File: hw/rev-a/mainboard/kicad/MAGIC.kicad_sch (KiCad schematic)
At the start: 16 parts, among them U7 SN74LVC4245APWR, U8 SN74LVC4245APWR, U9 SN74LVC4245APWR

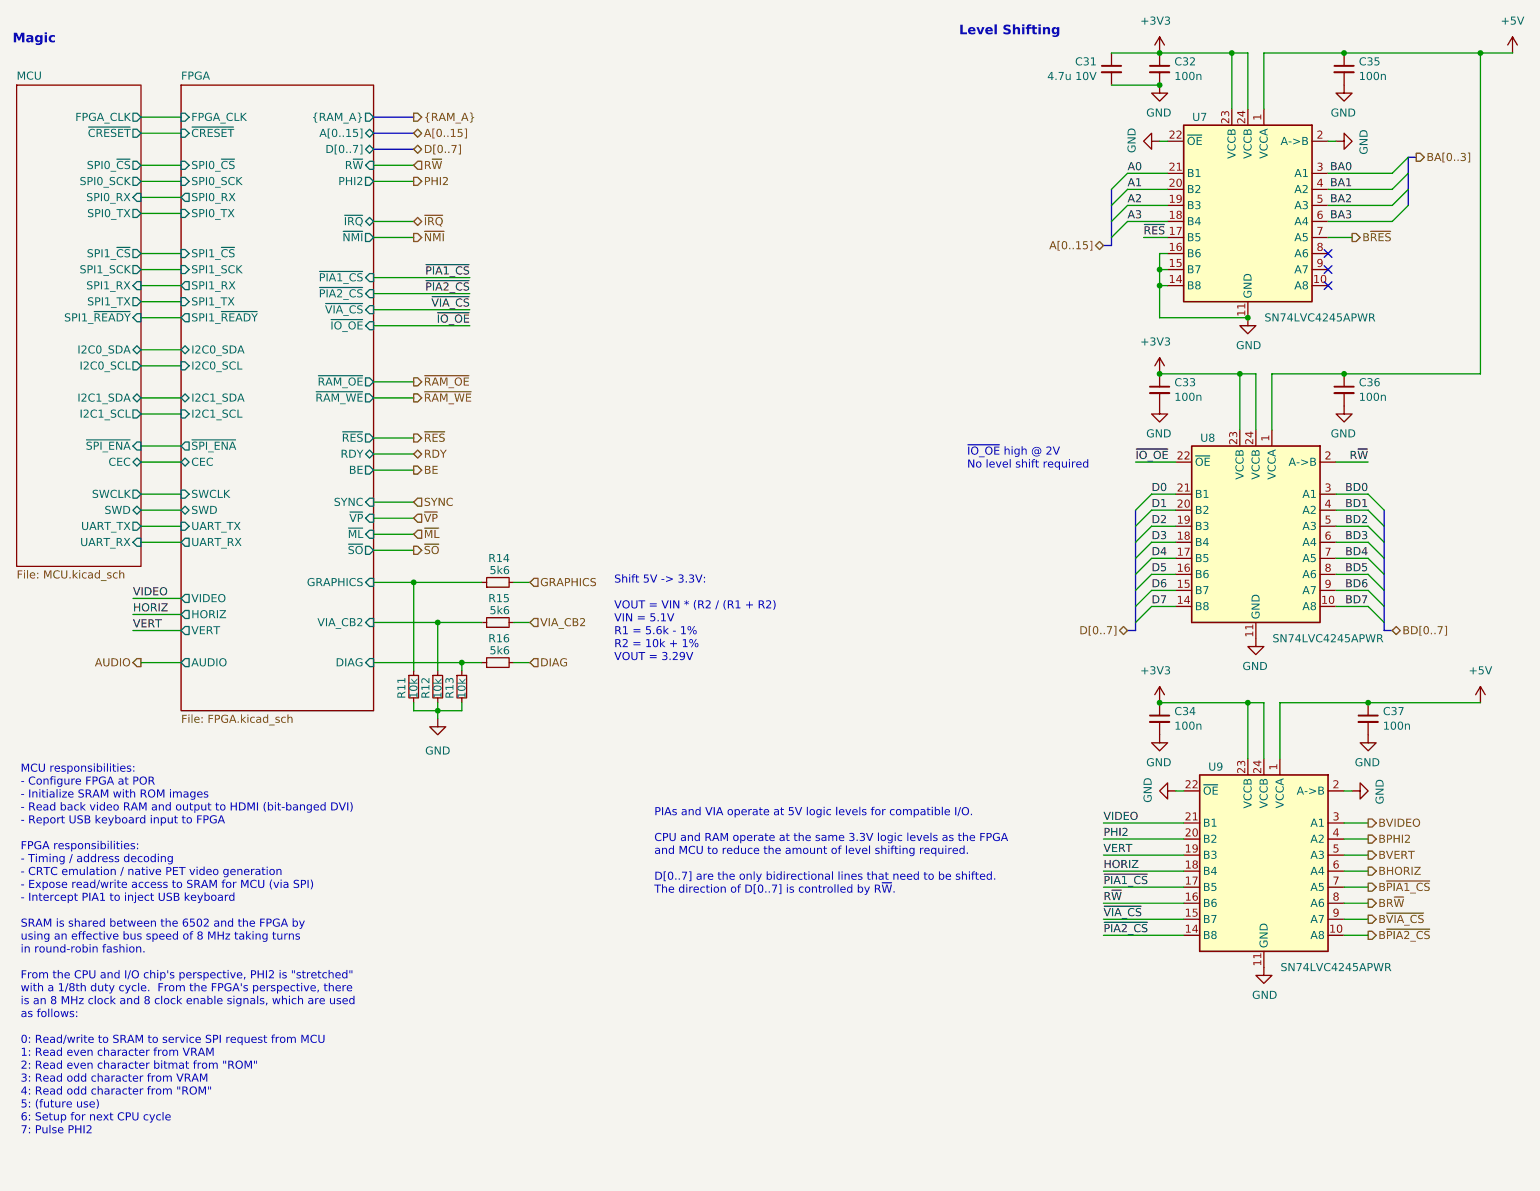
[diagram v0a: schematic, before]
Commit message: hw: ren rev-c -> rev-a
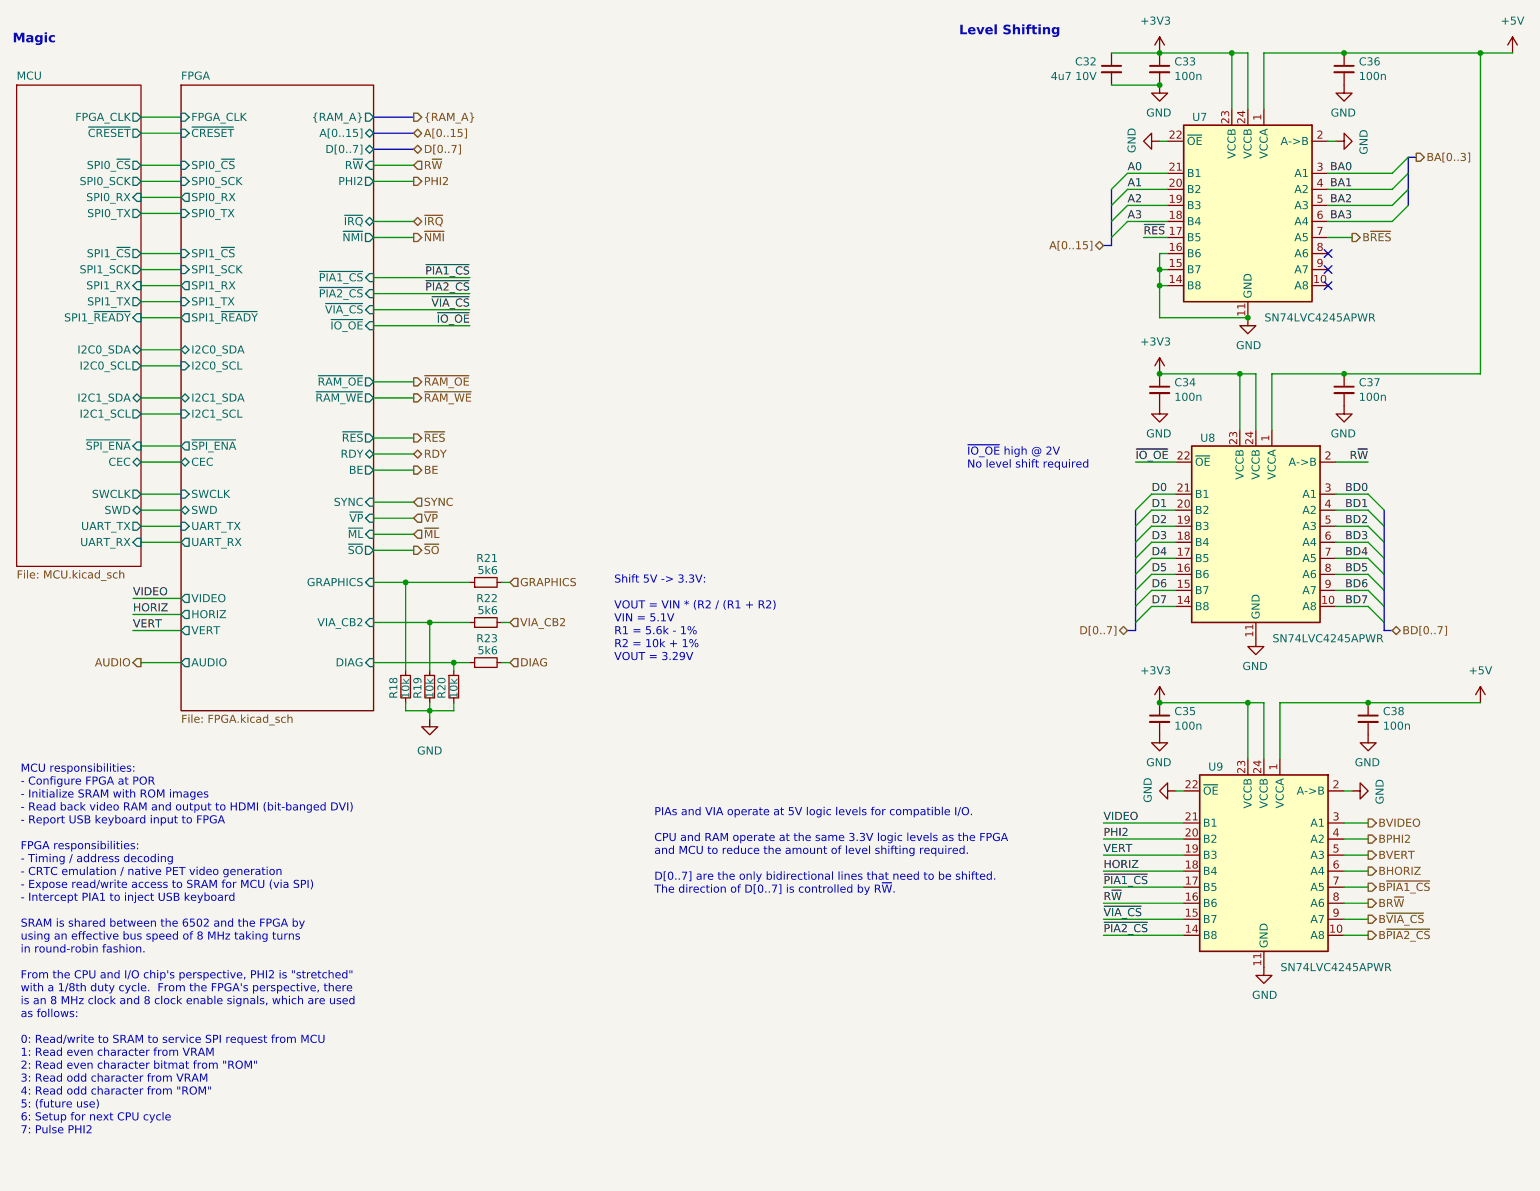
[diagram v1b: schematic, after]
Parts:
- C32: renamed from C31; value 4.7u 10V -> 4u7 10V
- U7, U8, U9: symbol Mainboard-rescue:SN74LVC8T245-PET -> EconoPET:SN74LVC8T245
- renumbered C32 to C33, C33 to C34, C34 to C35, C35 to C36, C36 to C37, C37 to C38, R11 to R18, R12 to R19, R13 to R20, R14 to R21, R15 to R22, R16 to R23
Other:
- moved on the sheet: R18, R19, R20, R21, R22, R23

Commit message: hw: tidy schematics for publication
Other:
- note added: "MCU responsibilities: - Generate FPGA_CLK - Configure FPGA at POR - Initialize SRAM with ROM images - Read back video RAM and output to HDMI (bit-banged DVI) - Report USB keyboard matrix to FPGA FPGA responsibilities: - Timing / address decoding - Native PET video generation / CRTC - Expose sysem bus to MCU (via SPI) - Intercept PIA1 to inject USB keyboard SRAM is shared between the 6502 and the 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"
- note added: "PIAs and VIA operate at 5V logic levels for compatible I/O. CPU and RAM operate at the same 3V3 logic levels as the FPGA and MCU to reduce the amount of level shifting required. D[0..7] are the only bidirectional lines that need to be shifted. The direction of D[0..7] is controlled by R~{W}."
- note added: "Shift 5V -> 3V3: VOUT = VIN * (R2 / (R1 + R2) VIN = 5.1V R1 = 5.6k - 1% R2 = 10k + 1% VOUT = 3.29V"
- note added: "~{IO_OE} does not require level-shifting (high @ 2V)"
- note removed: "MCU responsibilities: - Configure FPGA at POR - Initialize SRAM with ROM images - Read back video RAM and output to HDMI (bit-banged DVI) - Report USB keyboard input to FPGA FPGA responsibilities: - Timing / address decoding - CRTC emulation / native PET video generation - Expose read/write access to SRAM for MCU (via SPI) - Intercept PIA1 to inject USB keyboard SRAM is shared between the 6502 an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"
- note removed: "PIAs and VIA operate at 5V logic levels for compatible I/O. CPU and RAM operate at the same 3.3V logic levels as the FPGA and MCU to reduce the amount of level shifting required. D[0..7] are the only bidirectional lines that need to be shifted. The direction of D[0..7] is controlled by R~{W}."
- note removed: "Shift 5V -> 3.3V: VOUT = VIN * (R2 / (R1 + R2) VIN = 5.1V R1 = 5.6k - 1% R2 = 10k + 1% VOUT = 3.29V"
- note removed: "~{IO_OE} high @ 2V No level shift required"
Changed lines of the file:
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@@
 		(date "2023-10-01")
 		(rev "A")
+		(comment 1 "Unspecified resistors are 1% and rated for 62.5mW or higher")
+		(comment 2 "Unspecified capacitors are rated for 25V or higher")
+		(comment 3 "Signals with B-prefix are level-shifted from 3V3 to 5V")
 	)
 	(junction
@@
 		)
 	)
-	(text "PIAs and VIA operate at 5V logic levels for compatible I/O.\n\nCPU and RAM operate at the same 3.3V logic levels as the FPGA\nand MCU to reduce the amount of level shifting required.\n\nD[0..7] are the only bidirectional lines that need to be shifted.\nThe direction of D[0..7] is controlled by R~{W}."
+	(text "PIAs and VIA operate at 5V logic levels for compatible I/O.\n\nCPU and RAM operate at the same 3V3 logic levels as the FPGA\nand MCU to reduce the amount of level shifting required.\n\nD[0..7] are the only bidirectional lines that need to be shifted.\nThe direction of D[0..7] is controlled by R~{W}."
 		(exclude_from_sim no)
 		(at 127 153.67 0)
@@
 		)
 	)
-	(text "MCU responsibilities:\n- Configure FPGA at POR\n- Initialize SRAM with ROM images\n- Read back video RAM and output to HDMI (bit-banged DVI)\n- Report USB keyboard input to FPGA\n\nFPGA responsibilities:\n- Timing / address decoding\n- CRTC emulation / native PET video generation\n- Expose read/write access to SRAM for MCU (via SPI)\n- Intercept PIA1 to inject USB keyboard\n\nSRAM is shared between the 6502 and the FPGA by\nusing an effective bus speed of 8 MHz taking turns\nin round-robin fashion.\n\nFrom the CPU and I/O chip's perspective, PHI2 is \"stretched\"\nwith a 1/8th duty cycle.  From the FPGA's perspective, there\nis an 8 MHz clock and 8 clock enable signals, which are used\nas follows:\n\n0: Read/write to SRAM to service SPI request from MCU\n1: Read even character from VRAM\n2: Read even character bitmat from \"ROM\"\n3: Read odd character from VRAM\n4: Read odd character from \"ROM\"\n5: (future use)\n6: Setup for next CPU cycle\n7: Pulse PHI2"
+	(text "MCU responsibilities:\n- Generate FPGA_CLK\n- Configure FPGA at POR\n- Initialize SRAM with ROM images\n- Read back video RAM and output to HDMI (bit-banged DVI)\n- Report USB keyboard matrix to FPGA\n\nFPGA responsibilities:\n- Timing / address decoding\n- Native PET video generation / CRTC\n- Expose sysem bus to MCU (via SPI)\n- Intercept PIA1 to inject USB keyboard\n\nSRAM is shared between the 6502 and the FPGA by using an\neffective bus speed of 8 MHz taking turns in round-robin\nfashion.\n\nFrom the CPU and I/O chip's perspective, PHI2 is \"stretched\"\nwith a 1/8th duty cycle.  From the FPGA's perspective, there\nis an 8 MHz clock and 8 clock enable signals, which are used\nas follows:\n\n0: Read/write to SRAM to service SPI request from MCU\n1: Read even character from VRAM\n2: Read even character bitmat from \"ROM\"\n3: Read odd character from VRAM\n4: Read odd character from \"ROM\"\n5: Read/write to SRAM to service SPI request from MCU\n6: Setup for next CPU cycle\n7: Pulse PHI2\n\n(Note: Above subject to change with firmware updates.)"
 		(exclude_from_sim no)
-		(at 26.67 191.77 0)
+		(at 26.67 198.12 0)
 		(effects
 			(font
@@
 		)
 	)
-	(text "~{IO_OE} high @ 2V\nNo level shift required"
+	(text "~{IO_OE} does not require level-shifting\n(high @ 2V)"
 		(exclude_from_sim no)
-		(at 176.53 86.36 0)
+		(at 163.83 85.09 0)
 		(effects
 			(font
@@
 		)
 	)
-	(text "Shift 5V -> 3.3V:\n\nVOUT = VIN * (R2 / (R1 + R2)\nVIN = 5.1V\nR1 = 5.6k - 1%\nR2 = 10k + 1%\nVOUT = 3.29V"
+	(text "Shift 5V -> 3V3:\n\nVOUT = VIN * (R2 / (R1 + R2)\nVIN = 5.1V\nR1 = 5.6k - 1%\nR2 = 10k + 1%\nVOUT = 3.29V"
 		(exclude_from_sim no)
 		(at 120.65 116.84 0)

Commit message: hw: tidy schematics for publication
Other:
- company: (none) -> https://is.gd/6hpvh6
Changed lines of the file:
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@@
 		(date "2023-10-01")
 		(rev "A")
-		(comment 1 "Unspecified resistors are 1% and rated for 62.5mW or higher")
-		(comment 2 "Unspecified capacitors are rated for 25V or higher")
+		(company "https://is.gd/6hpvh6")
+		(comment 1 "Unspecified resistors are 1% / 62.5mW")
+		(comment 2 "Unspecified capacitors are 25V")
 		(comment 3 "Signals with B-prefix are level-shifted from 3V3 to 5V")
+		(comment 4 "License: CC0 1.0 Universal (Public Domain Dedication)")
 	)
 	(junction

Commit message: hw: tidy schematics for publication
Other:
- note added: "PIAs and VIA operate at 5V logic levels for compatible I/O. To reduce the amount of level shifting required, CPU and RAM operate at 3V3 logic levels to share the system bus with the FPGA. D[0..7] are the only bidirectional lines that need to be shifted. The direction of D[0..7] is controlled by R~{W}."
- note added: "~{IO_OE} is asserted whenenver address decoding asserts ~{PIA1_CS}, ~{PIA2_CS}, or ~{VIA_CS}. ~{IO_OE} does not require level-shifting (high @ 2V)"
- note removed: "PIAs and VIA operate at 5V logic levels for compatible I/O. CPU and RAM operate at the same 3V3 logic levels as the FPGA and MCU to reduce the amount of level shifting required. D[0..7] are the only bidirectional lines that need to be shifted. The direction of D[0..7] is controlled by R~{W}."
- note removed: "~{IO_OE} does not require level-shifting (high @ 2V)"
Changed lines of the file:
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@@
 		)
 	)
-	(text "PIAs and VIA operate at 5V logic levels for compatible I/O.\n\nCPU and RAM operate at the same 3V3 logic levels as the FPGA\nand MCU to reduce the amount of level shifting required.\n\nD[0..7] are the only bidirectional lines that need to be shifted.\nThe direction of D[0..7] is controlled by R~{W}."
+	(text "PIAs and VIA operate at 5V logic\nlevels for compatible I/O.\n\nTo reduce the amount of level shifting\nrequired, CPU and RAM operate at 3V3\nlogic levels to share the system bus\nwith the FPGA.\n\nD[0..7] are the only bidirectional\nlines that need to be shifted.\n\nThe direction of D[0..7] is controlled\nby R~{W}."
 		(exclude_from_sim no)
-		(at 127 153.67 0)
+		(at 147.32 45.72 0)
 		(effects
 			(font
@@
 	(text "Level Shifting"
 		(exclude_from_sim no)
-		(at 175.26 17.78 0)
+		(at 147.32 17.78 0)
 		(effects
 			(font
@@
 		)
 	)
-	(text "~{IO_OE} does not require level-shifting\n(high @ 2V)"
+	(text "~{IO_OE} is asserted whenenver address\ndecoding asserts ~{PIA1_CS}, ~{PIA2_CS},\nor ~{VIA_CS}.\n\n~{IO_OE} does not require level-shifting\n(high @ 2V)"
 		(exclude_from_sim no)
-		(at 163.83 85.09 0)
+		(at 162.56 91.44 0)
 		(effects
 			(font
